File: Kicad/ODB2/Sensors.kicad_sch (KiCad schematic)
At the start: 19 parts, among them J4 RF2-04A-T-00-50-G, J5 RFM_Conn_Coaxial, U5 L76L-M33, U6 ICM-20948, U7 MS580301BA01-00, U9 RFM23BP-433-S2

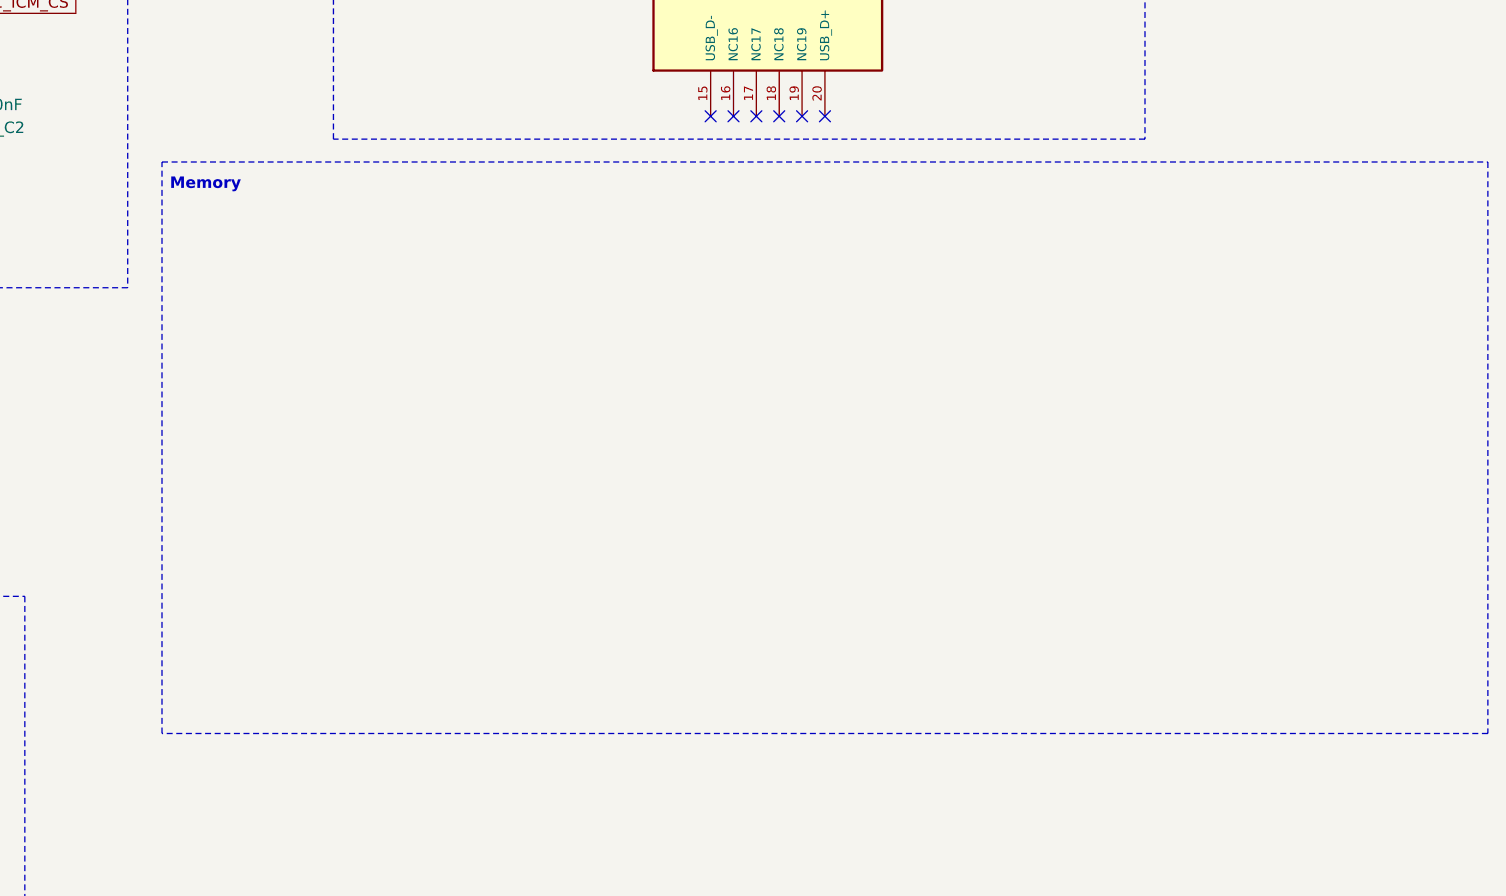
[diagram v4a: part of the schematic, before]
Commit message: delete hierarchie ODB
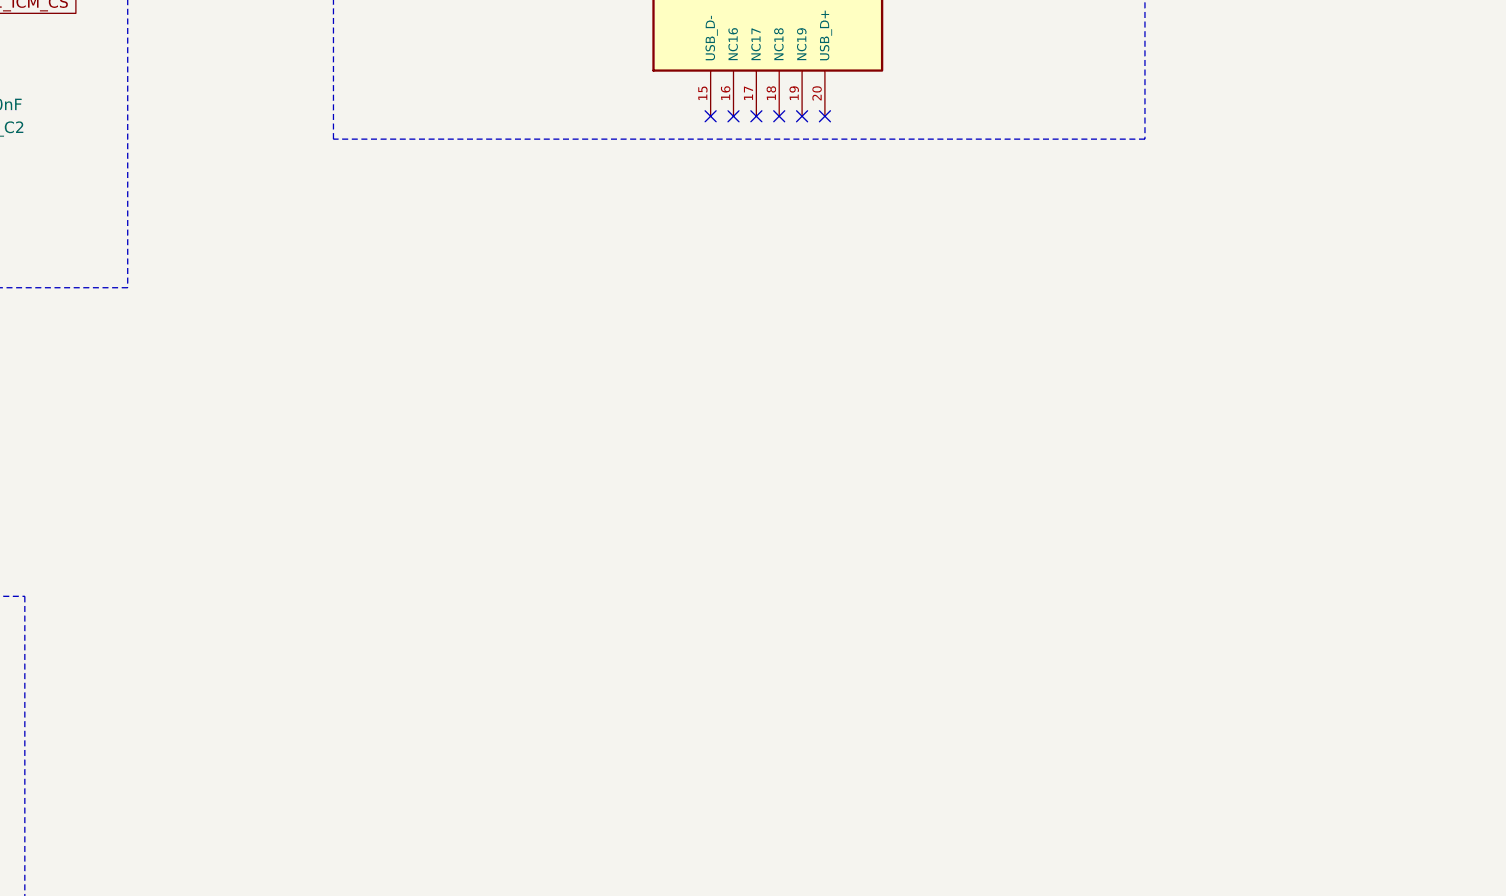
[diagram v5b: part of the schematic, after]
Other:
- note removed: "Memory"
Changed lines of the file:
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@@
-	)
-	(rectangle
-		(start 132.08 99.06)
-		(end 279.4 162.56)
-		(stroke
-			(width 0)
-			(type dash)
-		)
-		(fill
-			(type none)
-		)
 	)
 	(rectangle
@@
 		)
 	)
-	(text "Memory"
-		(exclude_from_sim no)
-		(at 136.906 101.6 0)
-		(effects
-			(font
-				(size 1.27 1.27)
-				(thickness 0.254)
-				(bold yes)
-			)
-		)
-	)

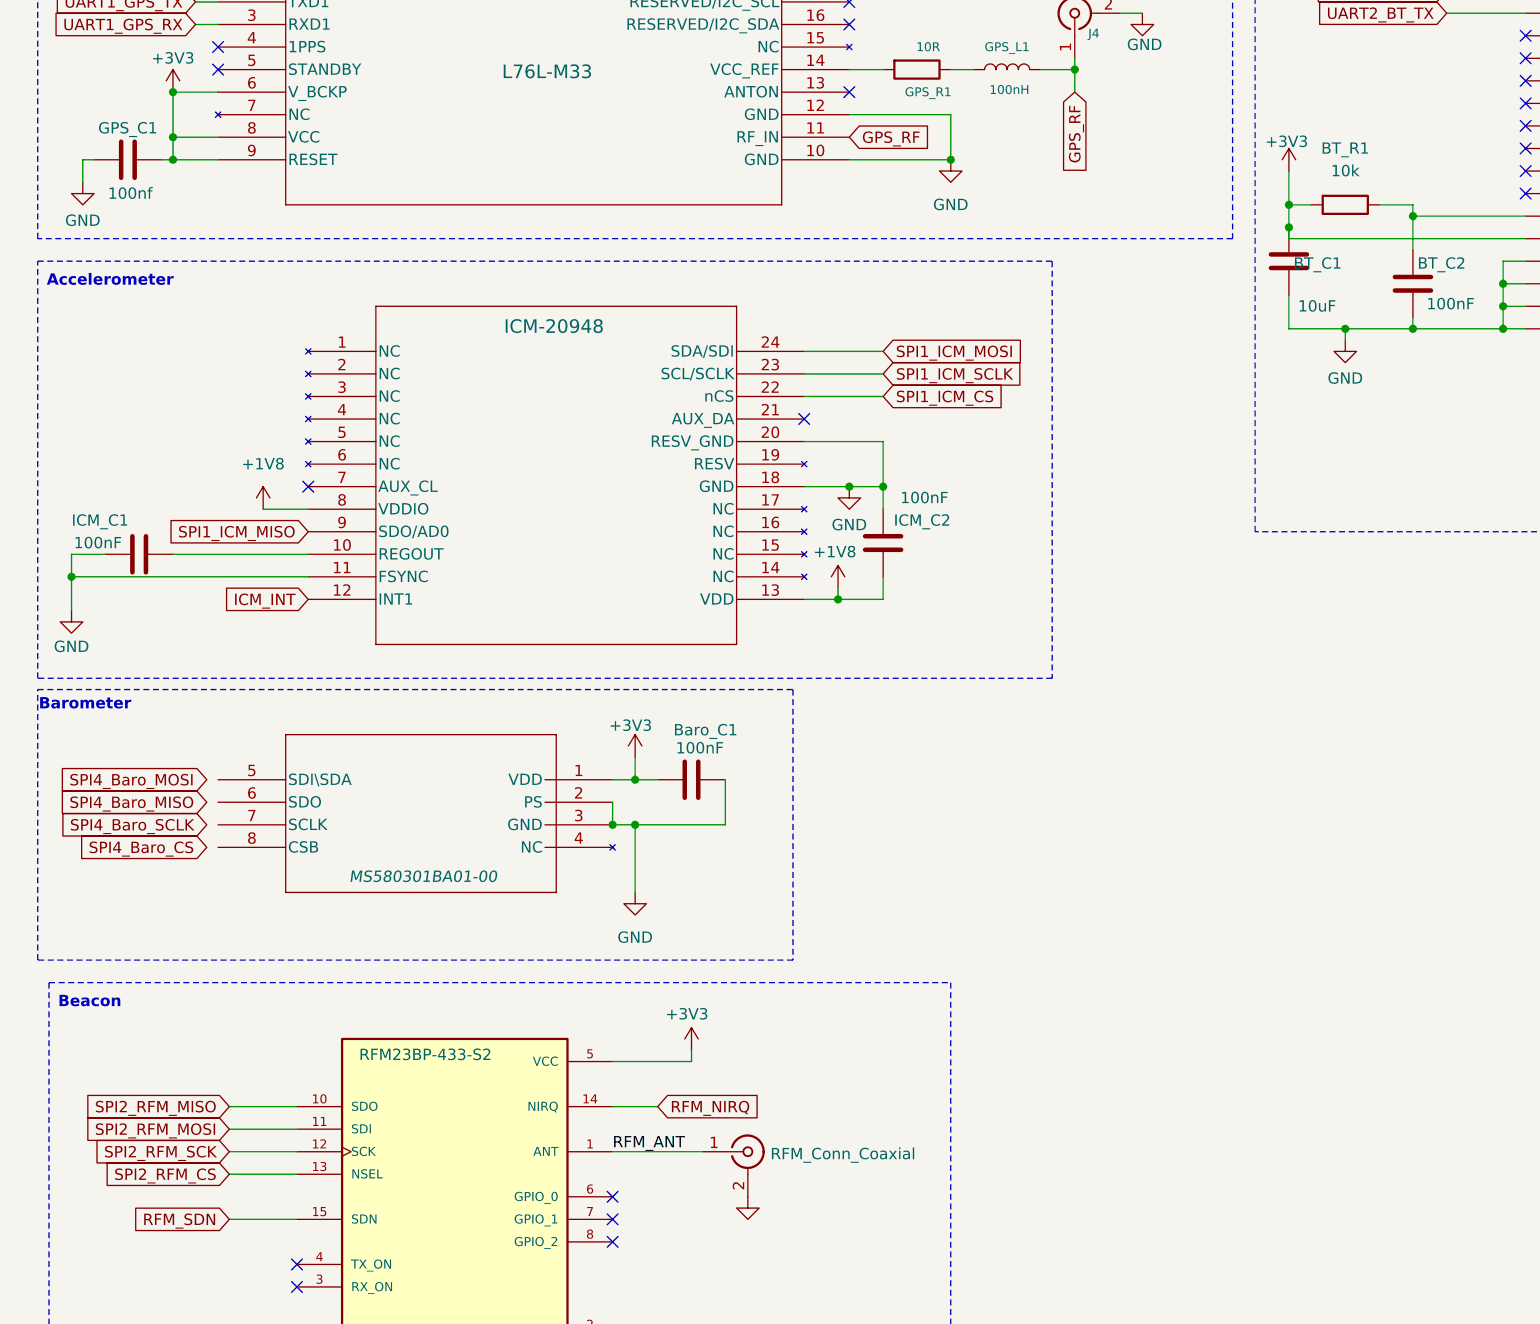
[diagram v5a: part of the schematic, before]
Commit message: add W25Q512JV
vérifier pinout communication
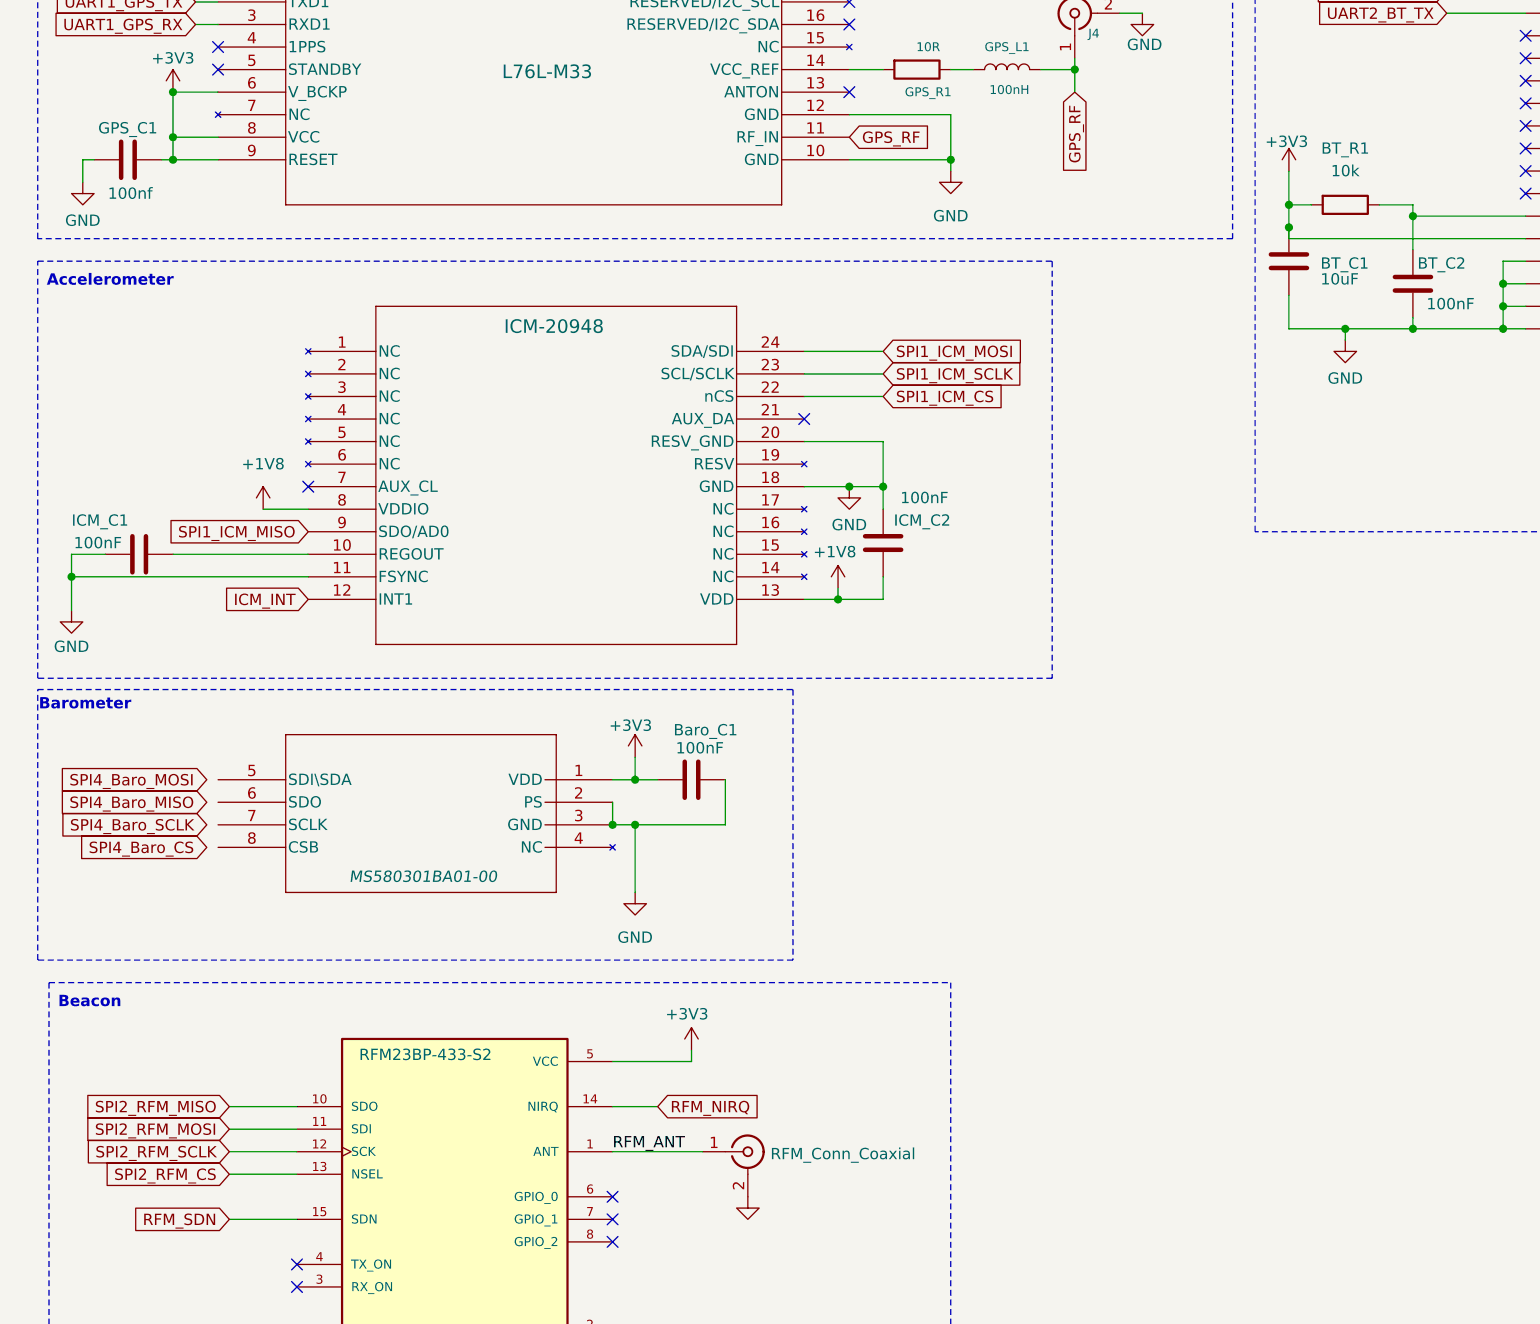
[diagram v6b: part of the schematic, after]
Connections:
- net SPI2_RFM_SCK renamed SPI2_RFM_SCLK
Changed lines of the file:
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@@
+	(wire
+		(pts
+			(xy 116.84 55.88) (xy 116.84 54.61)
+		)
+		(stroke
+			(width 0)
+			(type default)
+		)
+	)
 	(wire
 		(pts
@@
 		)
 	)
-	(global_label "SPI2_RFM_SCK"
+	(global_label "SPI2_RFM_SCLK"
 		(shape input)
 		(at 35.56 166.37 180)
@@
 		)
 		(property "Intersheetrefs" "${INTERSHEET_REFS}"
-			(at 18.7863 166.37 0)
+			(at 17.7582 166.37 0)
 			(effects
 				(font
@@
 		(dnp no)
 		(property "Reference" "BT_C1"
-			(at 155.448 66.294 0)
+			(at 158.496 66.294 0)
 			(effects
 				(font
@@
 		)
 		(property "Value" "10uF"
-			(at 155.956 71.12 0)
+			(at 158.496 68.072 0)
 			(effects
 				(font
@@
 	(symbol
 		(lib_id "power:GND")
-		(at 116.84 54.61 0)
+		(at 116.84 55.88 0)
 		(unit 1)
 		(exclude_from_sim no)
@@
 		(fields_autoplaced yes)
 		(property "Reference" "#PWR051"
+			(at 116.84 62.23 0)
+			(effects
+				(font
+					(size 1.27 1.27)
+				)
+				(hide yes)
+			)
+		)
+		(property "Value" "GND"
 			(at 116.84 60.96 0)
 			(effects
@@
 					(size 1.27 1.27)
 				)
-				(hide yes)
-			)
-		)
-		(property "Value" "GND"
-			(at 116.84 59.69 0)
-			(effects
-				(font
-					(size 1.27 1.27)
-				)
 			)
 		)
 		(property "Footprint" ""
-			(at 116.84 54.61 0)
+			(at 116.84 55.88 0)
 			(effects
 				(font
@@
 		)
 		(property "Datasheet" ""
-			(at 116.84 54.61 0)
+			(at 116.84 55.88 0)
 			(effects
 				(font
@@
 		)
 		(property "Description" "Power symbol creates a global label with name \"GND\" , ground"
-			(at 116.84 54.61 0)
-			(effects
-				(font
+			(at 116.84 55.88 0)
+			(effects
+				(font

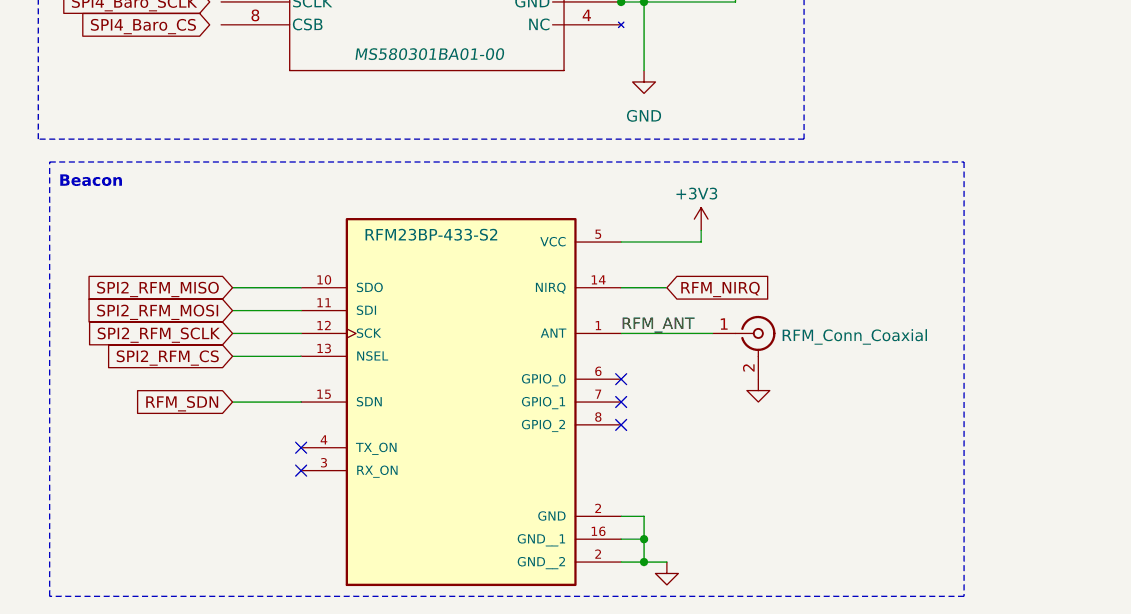
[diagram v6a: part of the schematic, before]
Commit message: fix circuit
reste à verifier les pinout
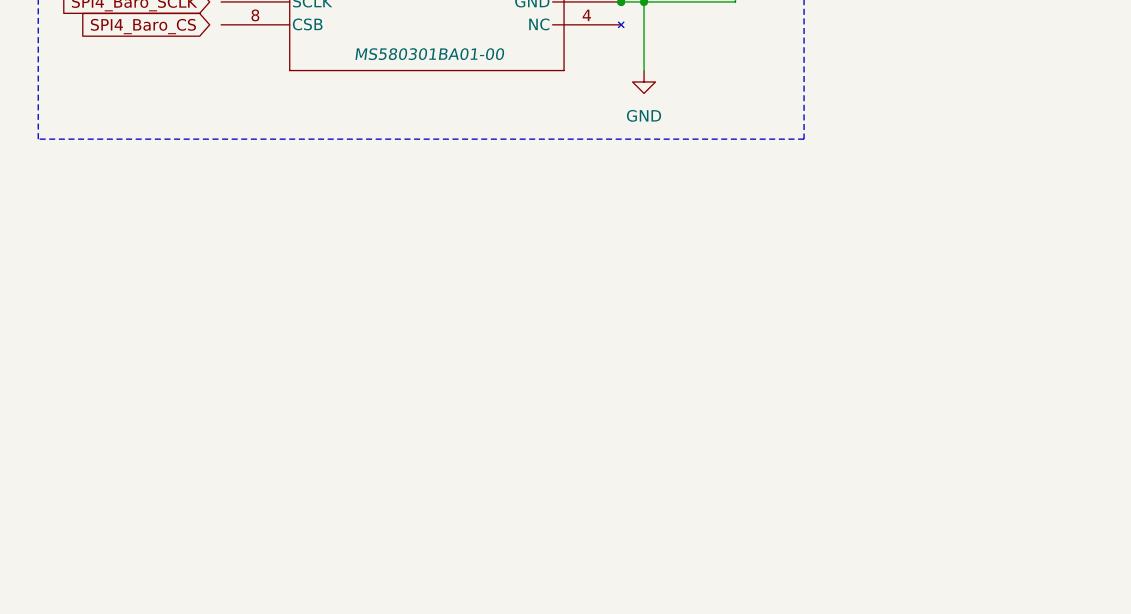
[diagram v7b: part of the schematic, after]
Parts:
- removed J5: RFM_Conn_Coaxial, symbol Connector:Conn_Coaxial
- removed U9: RFM23BP-433-S2, ODB:RFM22B-433-S2, symbol ODB2:RFM23BP-433-S2
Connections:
- no-connect marks 37 -> 32
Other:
- note removed: "Beacon"

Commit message: pyros (1er jet)
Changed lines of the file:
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@@
+		)
+	)
+	(text_box "Mettre bleu"
+		(exclude_from_sim no)
+		(at 226.06 45.72 0)
+		(size 12.7 5.08)
+		(stroke
+			(width 0)
+			(type default)
+		)
+		(fill
+			(type none)
+		)
+		(effects
+			(font
+				(size 1.27 1.27)
+			)
+			(justify left top)
 		)
 	)
